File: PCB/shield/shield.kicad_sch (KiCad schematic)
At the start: 14 parts, among them J1 QTR-8A, J13 Motor, J3 Servo, J4 Battery, Q1 SI2301DS, SW1 SW_SPST, U1 LM2596, U2 ESP32-S3-DevKitC, U3 TB6612FNG

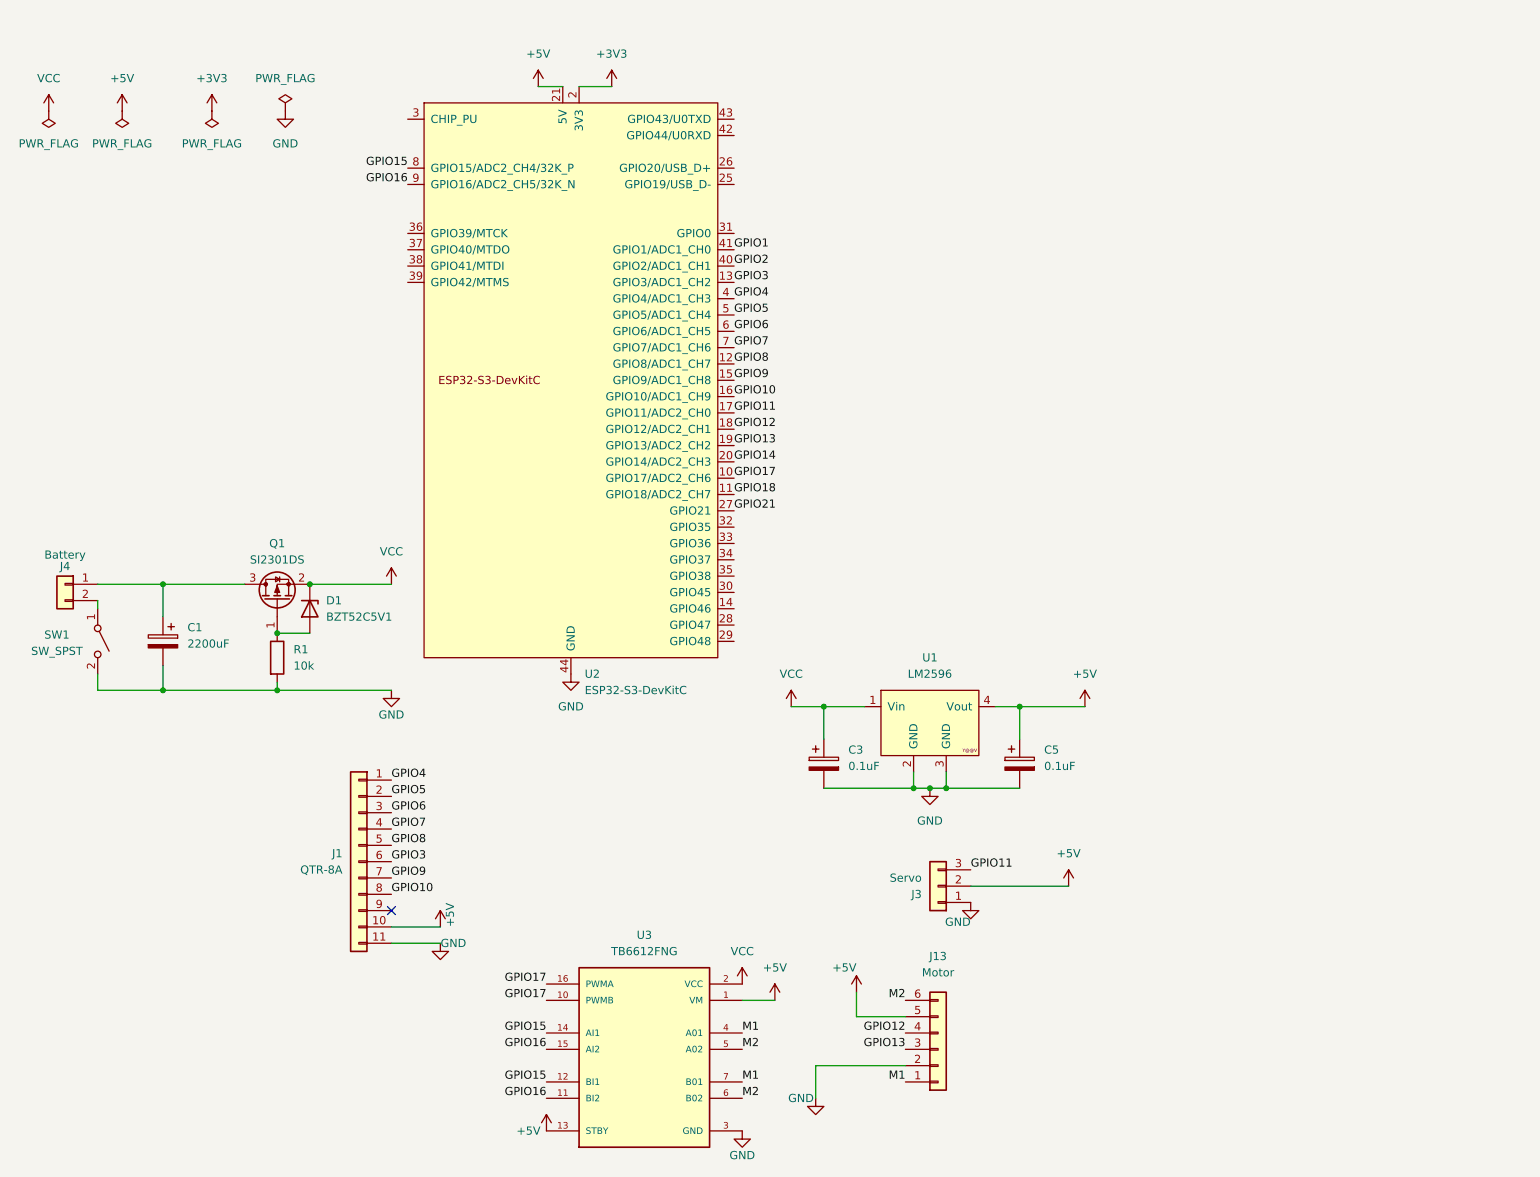
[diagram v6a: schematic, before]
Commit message: feat: change LM2596S to MP1584EN; change to 2-layer pcb
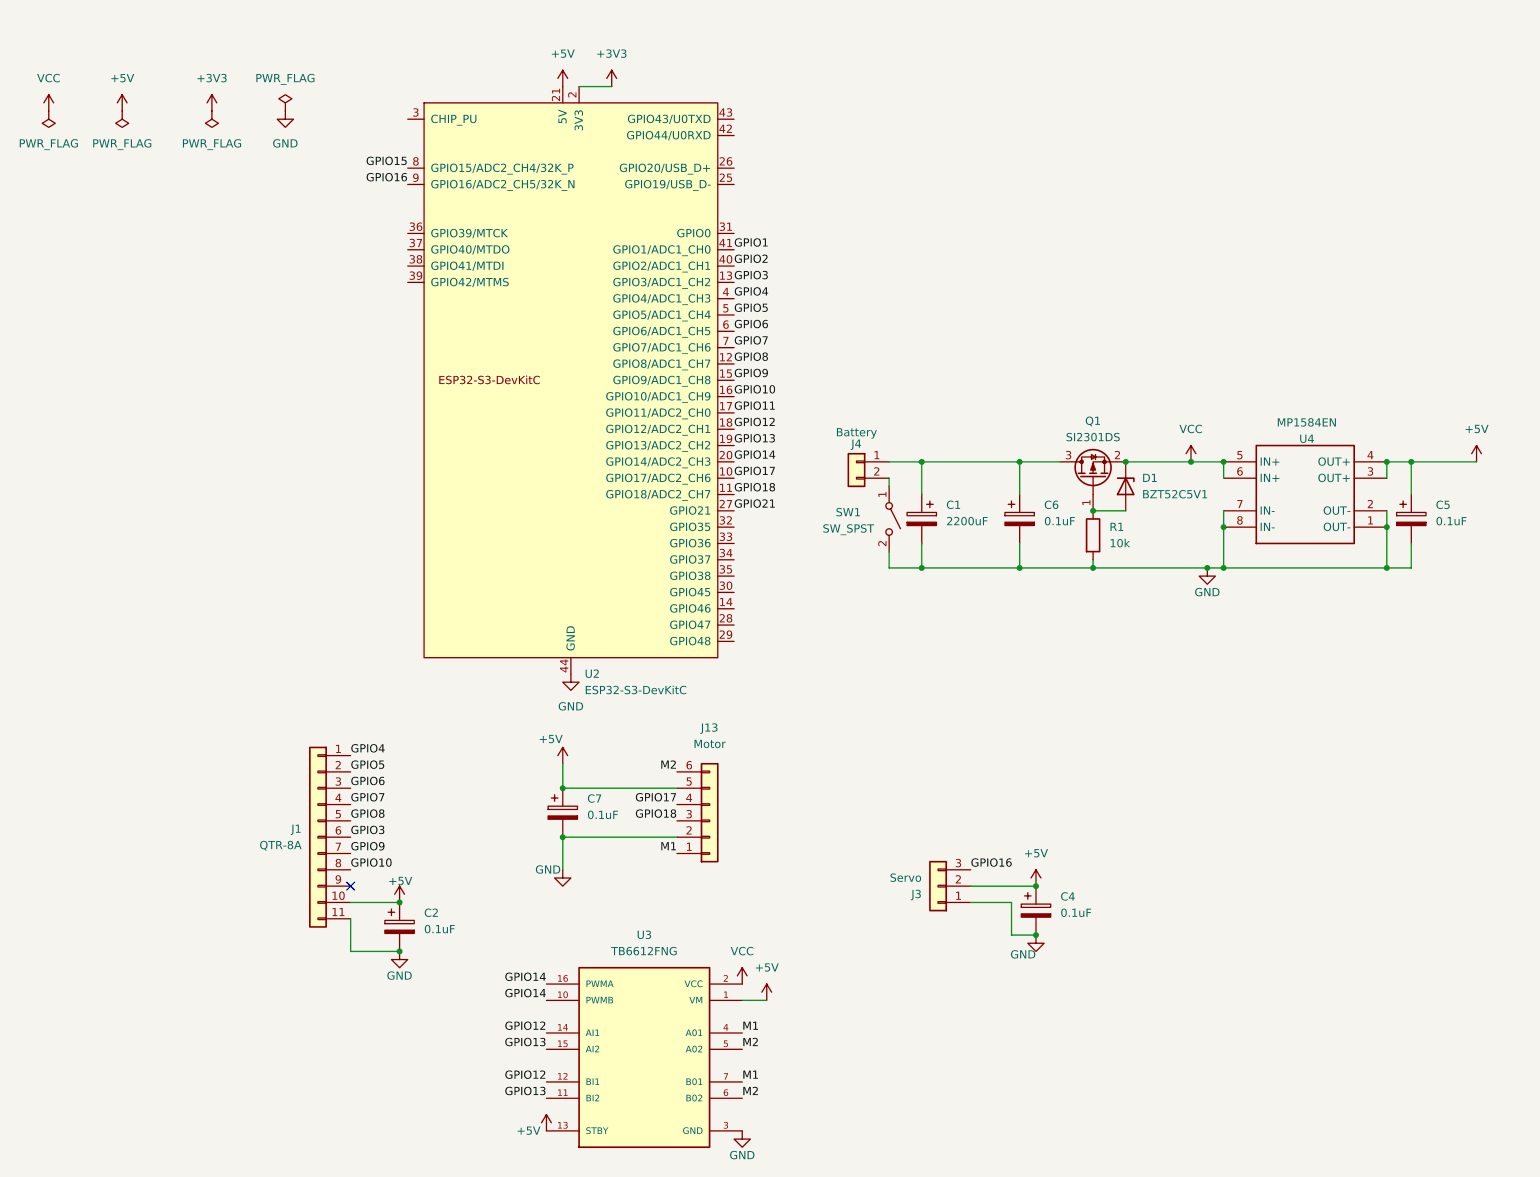
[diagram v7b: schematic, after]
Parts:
- removed C3: 0.1uF, Capacitor_SMD:C_0805_2012Metric_Pad1.18x1.45mm_HandSolder, symbol Device:C_Polarized
- removed U1: LM2596, KiCad:YAAJ_DCDC_StepDown_LM2596, symbol yaaj_dcdc_stepdown_lm2596:YAAJ_DCDC_StepDown_LM2596
- added C2, C4, C6, C7: 0.1uF, Capacitor_SMD:C_0805_2012Metric_Pad1.18x1.45mm_HandSolder, symbol Device:C_Polarized
- added U4: MP1584EN, MP1584EN:MP1584EN, symbol MP1584EN:MP1584EN
- SW1: footprint Rocket Switch:SW_RF1-1A-DC-2-R-1 -> RF1-1A-DC-2-R-1:SW_RF1-1A-DC-2-R-1
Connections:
- net +5V: now also C2.1, C4.1, C7.1, U4.3 (OUT+), U4.4 (OUT+)
- net GND: now also C2.2, C4.2, C6.2, C7.2, U4.1 (OUT-), U4.2 (OUT-), U4.7 (IN-), U4.8 (IN-)
- net GPIO11: no longer J3.3 (Pin_3)
- net GPIO12: now also U3.12 (BI1), U3.14 (AI1); no longer J13.4 (Pin_4)
- net GPIO13: now also U3.11 (BI2), U3.15 (AI2); no longer J13.3 (Pin_3)
- net GPIO14: now also U3.10 (PWMB), U3.16 (PWMA)
- net GPIO15: no longer U3.12 (BI1), U3.14 (AI1)
- net GPIO16: now also J3.3 (Pin_3); no longer U3.11 (BI2), U3.15 (AI2)
- net GPIO17: now also J13.4 (Pin_4); no longer U3.10 (PWMB), U3.16 (PWMA)
- net GPIO18: now also J13.3 (Pin_3)
- net VCC: now also U4.5 (IN+), U4.6 (IN+)
- net at C1.1, J4.1 (Pin_1), Q1.3 (D): now also C6.1
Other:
- moved on the sheet: C1, C5, D1, J1, J13, J4, Q1, R1, SW1

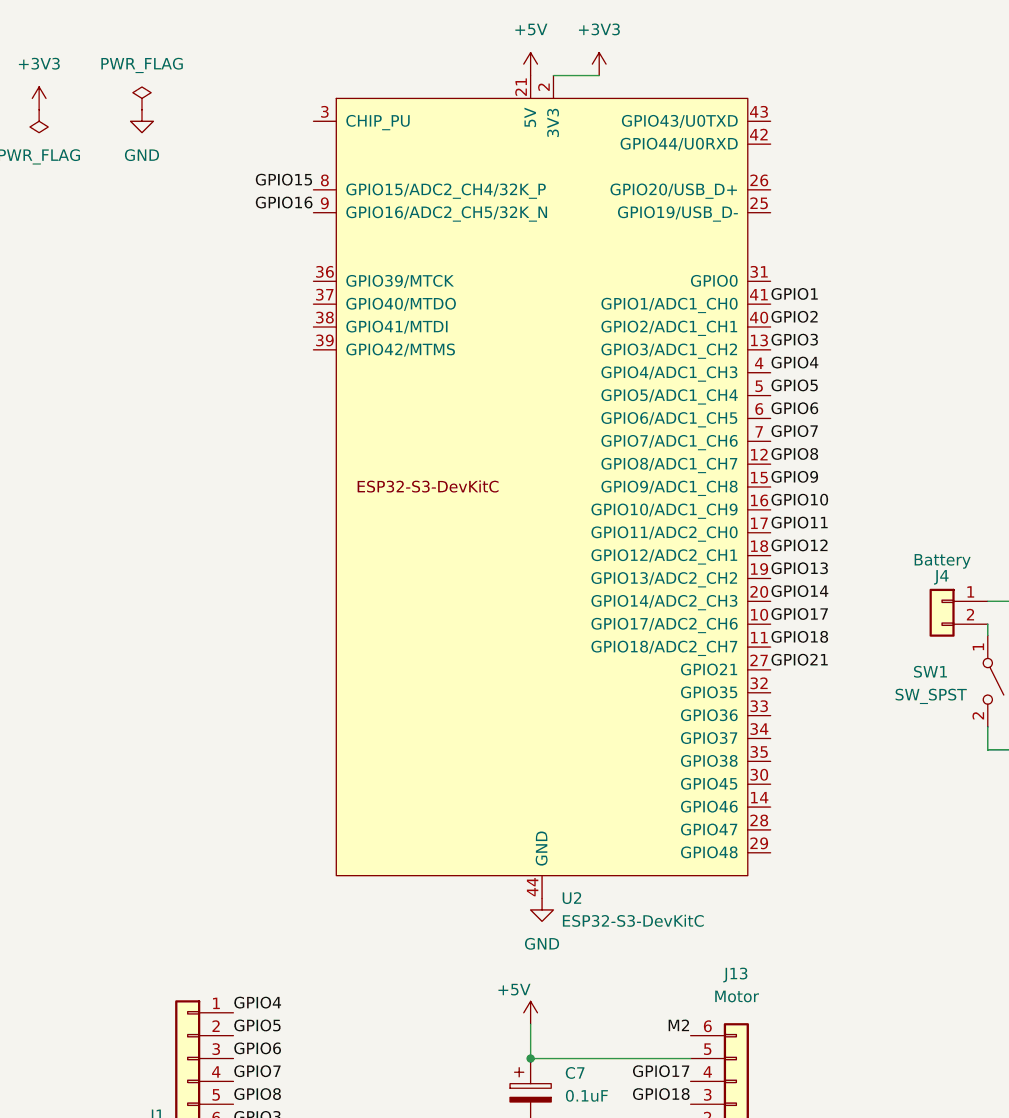
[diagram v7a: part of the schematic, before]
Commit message: feat: change esp32 footprint using altium-based lib
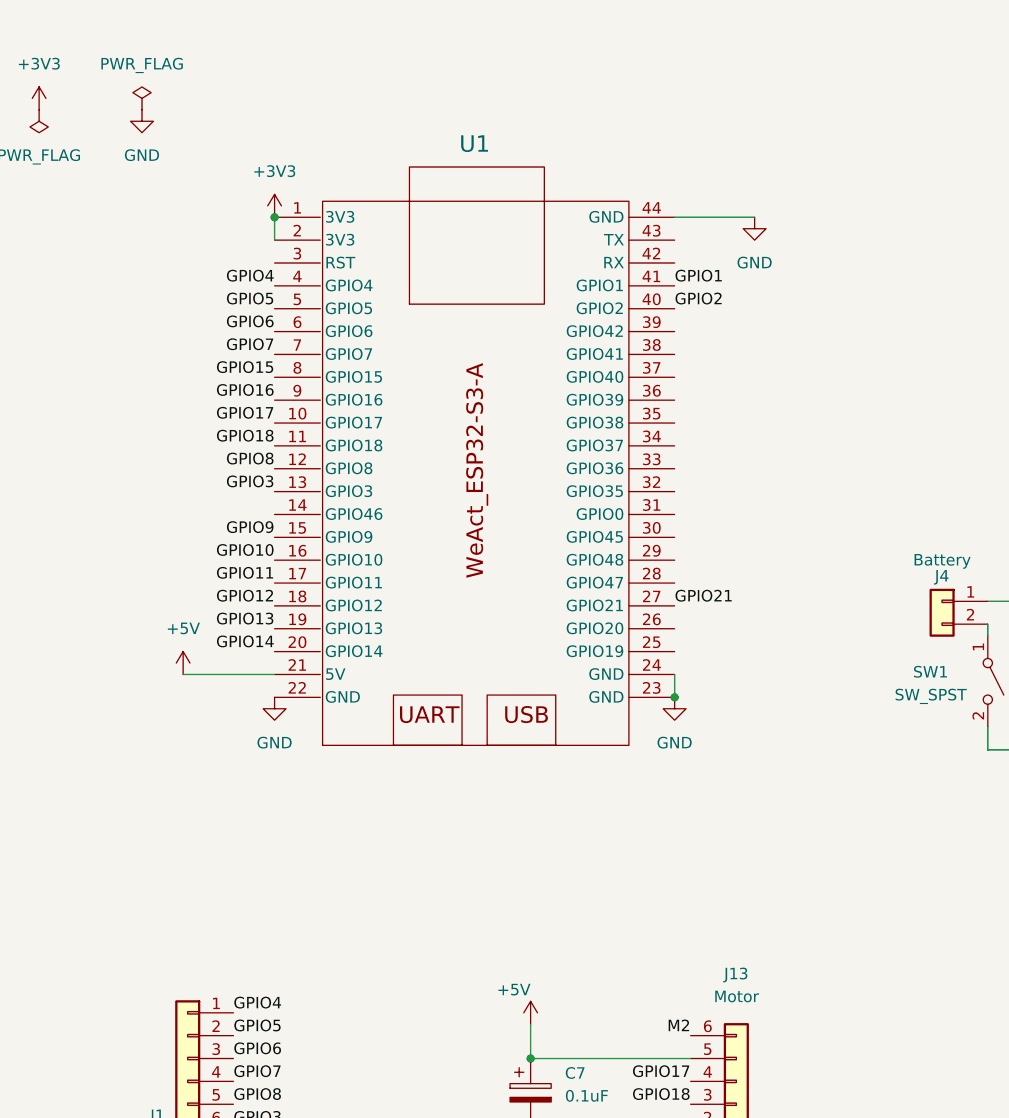
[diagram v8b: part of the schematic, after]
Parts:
- removed U2: ESP32-S3-DevKitC, PCM_Espressif:ESP32-S3-DevKitC, symbol PCM_Espressif:ESP32-S3-DevKitC
- added U1: WeAct-ESP32-S3-A, WeAct-ESP32-S3-A:WeAct-ESP32-S3-A, symbol WeAct-ESP32-S3-A:WeAct-ESP32-S3-A
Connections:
- net +3V3: now also U1.1 (3V3), U1.2 (3V3)
- net +5V: now also U1.21 (5V)
- net GND: now also U1.22 (GND), U1.23 (GND), U1.24 (GND), U1.44 (GND)
- net GPIO1: now also U1.41 (GPIO1)
- net GPIO10: now also U1.16 (GPIO10)
- net GPIO11: now also U1.17 (GPIO11)
- net GPIO12: now also U1.18 (GPIO12)
- net GPIO13: now also U1.19 (GPIO13)
- net GPIO14: now also U1.20 (GPIO14)
- net GPIO15: now also U1.8 (GPIO15)
- net GPIO16: now also U1.9 (GPIO16)
- net GPIO17: now also U1.10 (GPIO17)
- net GPIO18: now also U1.11 (GPIO18)
- net GPIO2: now also U1.40 (GPIO2)
- net GPIO21: now also U1.27 (GPIO21)
- net GPIO3: now also U1.13 (GPIO3)
- net GPIO4: now also U1.4 (GPIO4)
- net GPIO5: now also U1.5 (GPIO5)
- net GPIO6: now also U1.6 (GPIO6)
- net GPIO7: now also U1.7 (GPIO7)
- net GPIO8: now also U1.12 (GPIO8)
- net GPIO9: now also U1.15 (GPIO9)
